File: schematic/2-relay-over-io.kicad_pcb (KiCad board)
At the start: 2 copper layers, 86.4 x 51.4 mm, 26 parts, among them J2 Screw_Terminal_01x03, J3 Screw_Terminal_01x03, J5 Conn_02x05_Odd_Even, J6 Conn_02x05_Odd_Even, J7 Conn_02x08_Odd_Even, J8 Conn_02x08_Odd_Even, Q2 BC817, Q3 BC817, U2 SONGLE_3V_relay, U3 SONGLE_3V_relay, U6 DizzyBITLogo, U7 DizzyBIT-Layout

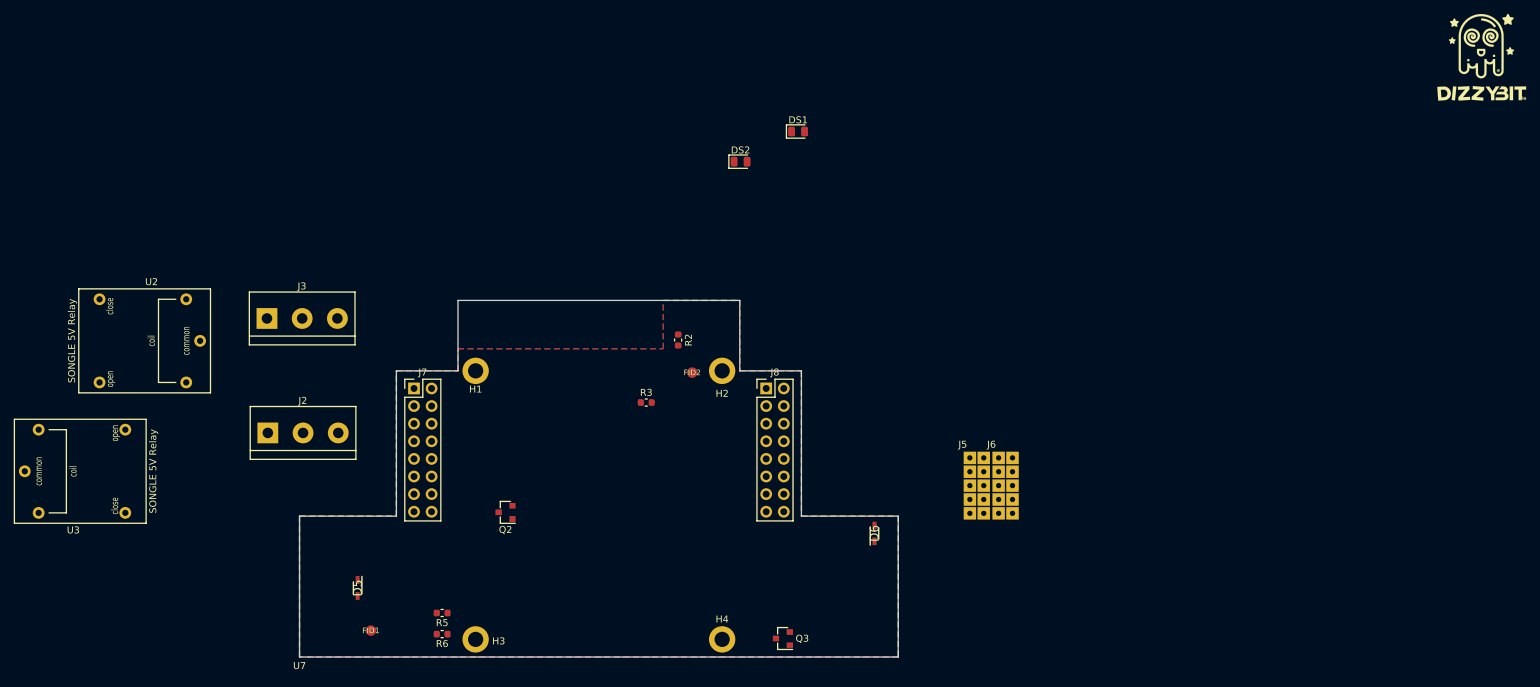
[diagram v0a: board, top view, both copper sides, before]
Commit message: Updated according to standard module design
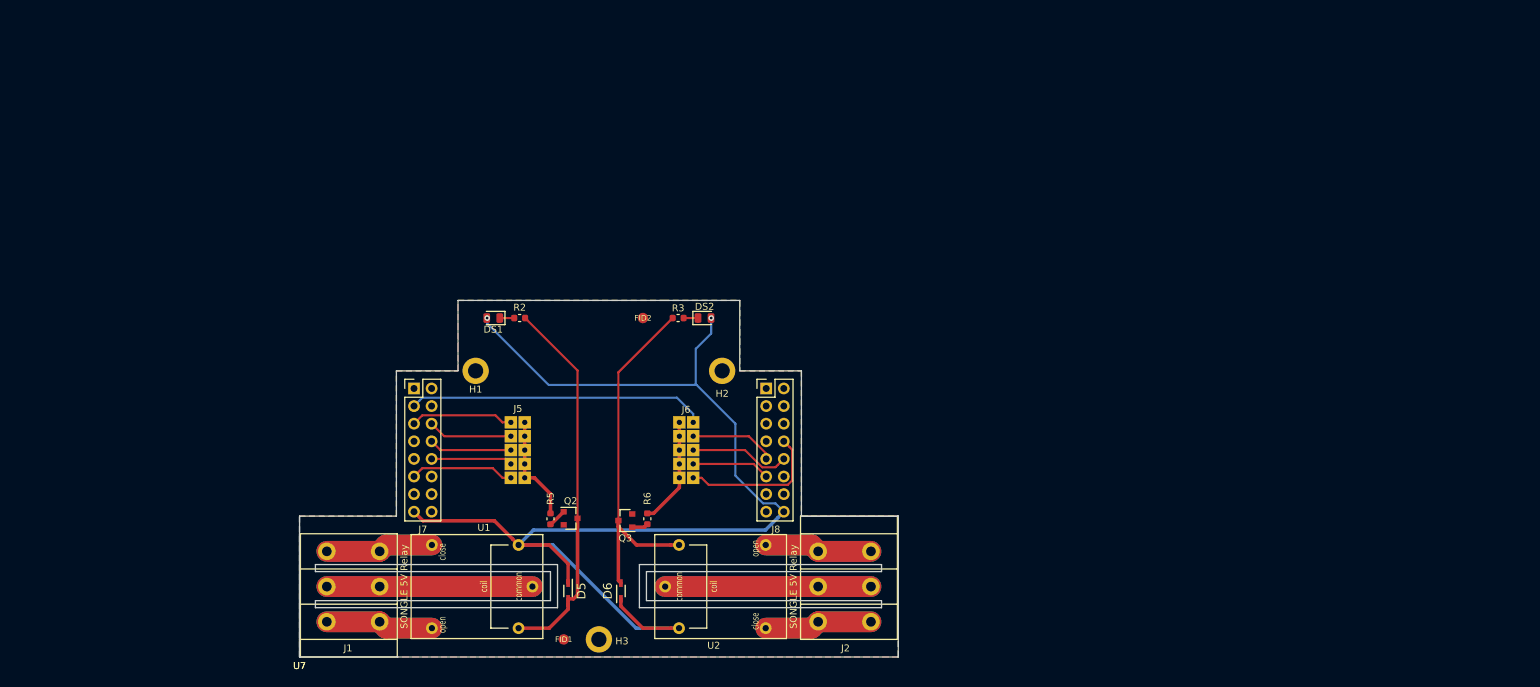
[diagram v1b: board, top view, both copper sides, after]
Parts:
- removed H4: MountingHole, MountingHole:MountingHole_2.2mm_M2_DIN965_Pad
- removed J3: Screw_Terminal_01x03, TerminalBlock:TerminalBlock_bornier-3_P5.08mm
- removed U3: SONGLE_3V_relay, Songle:SONGLE_5V_Relay
- removed the U7 at (76.2, 146.1)
- added J1: WJ142R-5.08-3P, TerminalBlock:WJ142R-5.08-3P, F.Cu at (90.3, 146.1)
- added U1: SONGLE_3V_relay, Songle:SONGLE_5V_Relay, F.Cu at (102.3, 135.4)
- added U7 (x2): DizzyBIT-Layout, DizzyBit:DizzyBit-Din Rail Module, F.Cu at (76.2, 146.1)
- J2: value Screw_Terminal_01x03 -> WJ142R-5.08-3P; footprint TerminalBlock:TerminalBlock_bornier-3_P5.08mm -> TerminalBlock:WJ142R-5.08-3P
- U6: moved to B.Cu
- moved U6 139.7 mm to (119.4, 117.0), turned to 180 degrees
- moved U2 89.8 mm to (136.4, 136.4), turned to 180 degrees
- moved J2 77.8 mm to (148.5, 125.7)
- moved J5 66.4 mm to (105.7, 111.2)
- moved DS1 51.6 mm to (104.1, 97.2), turned to 180 degrees
- moved J6 42.3 mm to (134.0, 121.2), turned to 180 degrees
- moved D6 37.5 mm to (122.6, 136.5)
- moved R6 33.9 mm to (126.4, 126.1), turned to 270 degrees
- moved D5 30.4 mm to (114.9, 136.5)
- moved Q3 28.4 mm to (123.2, 126.4)
- moved FID1 27.8 mm to (114.3, 143.5)
- moved DS2 23.1 mm to (134.6, 97.2)
- moved R2 23.1 mm to (108.0, 97.2), turned to 180 degrees
- moved R5 20.7 mm to (112.4, 126.1), turned to 270 degrees
- moved H3 17.8 mm to (119.4, 143.5)
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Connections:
- U2 pad 2: Net-(D5-Pad2) -> Net-(D6-Pad2)
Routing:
- net +3V3: track 0.00 -> 177.4 mm, vias 0 -> 2
- net Net-(J2-Pad2): track 0.00 -> 59.4 mm
- net Net-(J1-Pad2): track 0.00 -> 59.3 mm
- net Net-(D5-Pad2): track 0.00 -> 54.7 mm
- net Net-(D6-Pad2): track 0.00 -> 52.4 mm
- net IO33: track 0.00 -> 43.0 mm
- net Net-(J2-Pad1): track 0.00 -> 31.1 mm
- net Net-(J2-Pad3): track 0.00 -> 31.1 mm
- net Net-(J1-Pad3): track 0.00 -> 31.1 mm
- net Net-(J1-Pad1): track 0.00 -> 31.1 mm
- net IO5: track 0.00 -> 21.1 mm
- net RELAY2_CTR: track 0.00 -> 15.6 mm
- net RELAY1_CTR: track 0.00 -> 15.5 mm
- net IO15: track 0.00 -> 15.0 mm
- net IO26: track 0.00 -> 14.9 mm
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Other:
- outline, holes or cut-outs redrawn
- board text added: "2 Relay Module"
- board text added: "IO04"
- board text added: "IO05"
- board text added: "IO15"
- board text added: "IO16"
- board text added: "IO17"
- board text added: "IO25"
- board text added: "IO26"
- board text added: "IO27"
- board text added: "IO32"
- board text added: "IO33"
- board text added: "Relay 1 Control"
- board text added: "Relay 2 Control"
- board text removed: "ESP32D MCU"

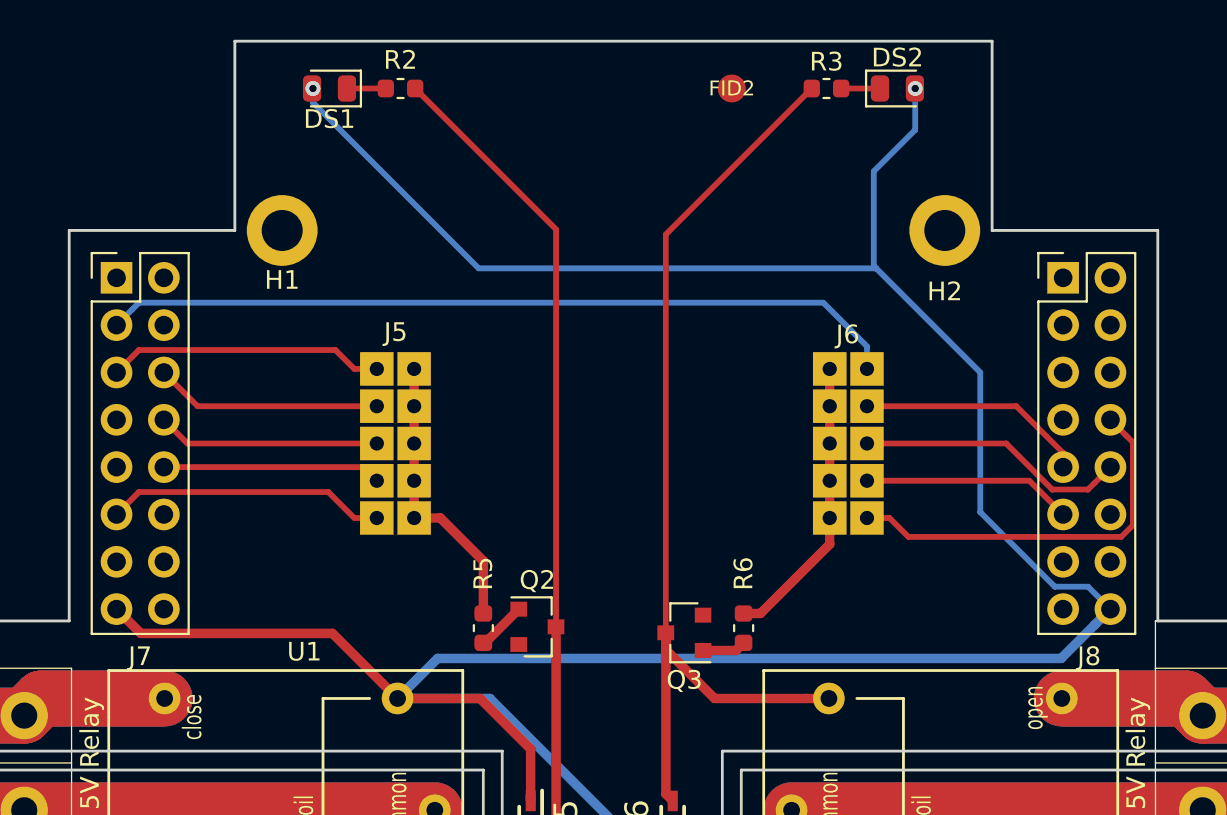
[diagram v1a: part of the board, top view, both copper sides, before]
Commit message: Updated 3.3v position and tracks
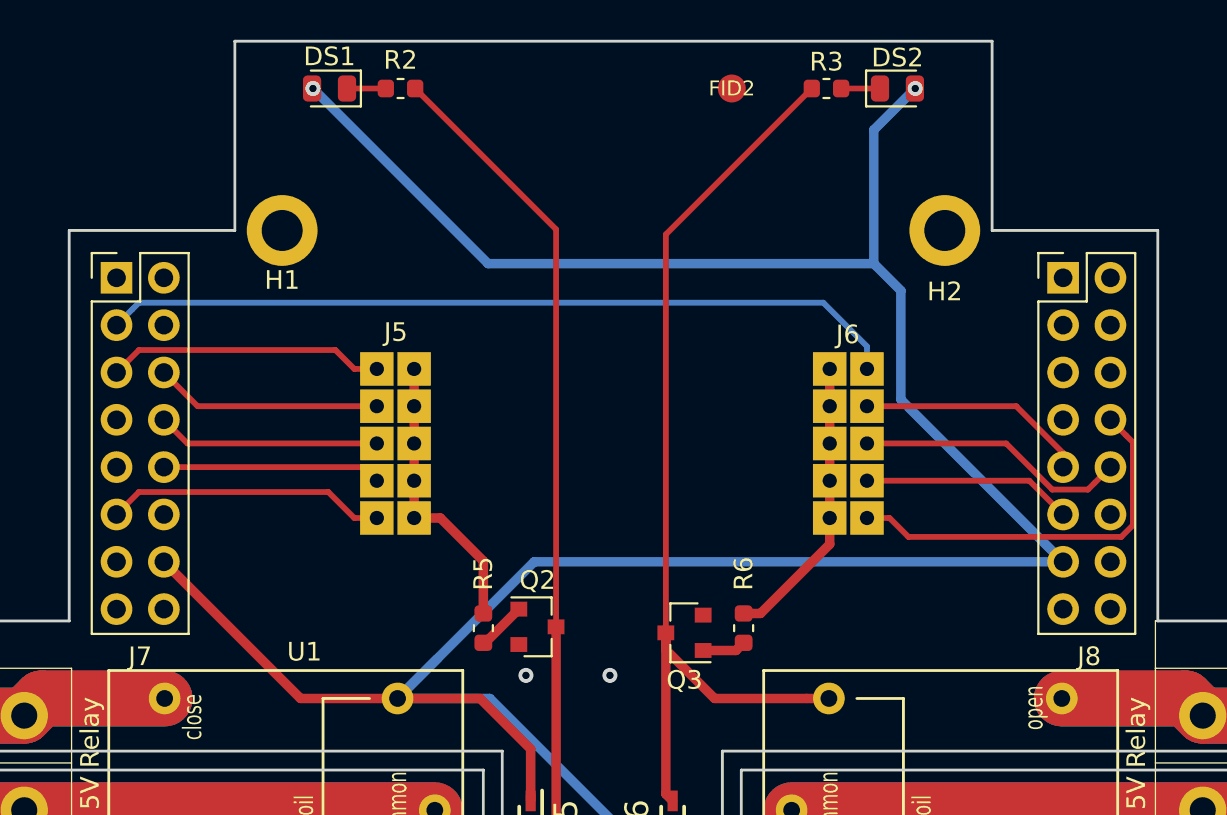
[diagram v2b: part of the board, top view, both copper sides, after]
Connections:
- J7 pad 14: (no net) -> +3V3
- J7 pad 15: +3V3 -> (no net)
- J8 pad 13: (no net) -> +3V3
- J8 pad 16: +3V3 -> (no net)
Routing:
- net +3V3: track 177.4 -> 172.4 mm
- net GND: vias 0 -> 2
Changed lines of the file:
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@@
-(kicad_pcb (version 20171130) (host pcbnew "(5.1.0)-1")
+(kicad_pcb (version 20171130) (host pcbnew "(5.0.2)-1")
   (general
     (thickness 1.6)
     (drawings 41)
-    (tracks 129)
+    (tracks 125)
     (zones 0)
     (modules 26)
@@
     (47 F.CrtYd user)
     (48 B.Fab user hide)
-    (49 F.Fab user)
+    (49 F.Fab user hide)
   )
   (setup
-    (last_trace_width 0.25)
+    (last_trace_width 0.508)
     (user_trace_width 0.254)
     (user_trace_width 0.31)
@@
     (zone_45_only no)
     (trace_min 0.2)
+    (segment_width 0.2)
+    (edge_width 0.15)
     (via_size 0.8)
     (via_drill 0.4)
@@
     (uvia_min_size 0.2)
     (uvia_min_drill 0.1)
-    (edge_width 0.15)
-    (segment_width 0.2)
     (pcb_text_width 0.3)
     (pcb_text_size 1.5 1.5)
@@
     (tags diode)
     (attr smd)
-    (fp_text reference DS1 (at 0 -1.65 180) (layer F.SilkS)
+    (fp_text reference DS1 (at 0 1.7145 180) (layer F.SilkS)
       (effects (font (size 1 1) (thickness 0.15)))
     )
@@
     (pad 12 thru_hole oval (at 2.54 12.7) (size 1.7 1.7) (drill 1) (layers *.Cu *.Mask))
     (pad 13 thru_hole oval (at 0 15.24) (size 1.7 1.7) (drill 1) (layers *.Cu *.Mask))
-    (pad 14 thru_hole oval (at 2.54 15.24) (size 1.7 1.7) (drill 1) (layers *.Cu *.Mask))
-    (pad 15 thru_hole oval (at 0 17.78) (size 1.7 1.7) (drill 1) (layers *.Cu *.Mask)
+    (pad 14 thru_hole oval (at 2.54 15.24) (size 1.7 1.7) (drill 1) (layers *.Cu *.Mask)
       (net 23 +3V3))
+    (pad 15 thru_hole oval (at 0 17.78) (size 1.7 1.7) (drill 1) (layers *.Cu *.Mask))
     (pad 16 thru_hole oval (at 2.54 17.78) (size 1.7 1.7) (drill 1) (layers *.Cu *.Mask)
       (net 1 GND))
@@
     (fp_line (start 3.81 -1.27) (end 3.81 19.05) (layer F.Fab) (width 0.1))
     (fp_line (start 0 -1.27) (end 3.81 -1.27) (layer F.Fab) (width 0.1))
-    (pad 16 thru_hole oval (at 2.54 17.78) (size 1.7 1.7) (drill 1) (layers *.Cu *.Mask)
-      (net 23 +3V3))
+    (pad 16 thru_hole oval (at 2.54 17.78) (size 1.7 1.7) (drill 1) (layers *.Cu *.Mask))
     (pad 15 thru_hole oval (at 0 17.78) (size 1.7 1.7) (drill 1) (layers *.Cu *.Mask)
       (net 1 GND))
     (pad 14 thru_hole oval (at 2.54 15.24) (size 1.7 1.7) (drill 1) (layers *.Cu *.Mask))
-    (pad 13 thru_hole oval (at 0 15.24) (size 1.7 1.7) (drill 1) (layers *.Cu *.Mask))
+    (pad 13 thru_hole oval (at 0 15.24) (size 1.7 1.7) (drill 1) (layers *.Cu *.Mask)
+      (net 23 +3V3))
     (pad 12 thru_hole oval (at 2.54 12.7) (size 1.7 1.7) (drill 1) (layers *.Cu *.Mask))
     (pad 11 thru_hole oval (at 0 12.7) (size 1.7 1.7) (drill 1) (layers *.Cu *.Mask)
@@
   (gr_line (start 162.56 146.05) (end 162.56 125.73) (layer Edge.Cuts) (width 0.15))
   (gr_line (start 76.2 146.05) (end 162.56 146.05) (layer Edge.Cuts) (width 0.15))
+  (via (at 119.1895 128.651) (size 0.8) (drill 0.4) (layers F.Cu B.Cu) (net 1))
+  (via (at 114.681 128.651) (size 0.8) (drill 0.4) (layers F.Cu B.Cu) (net 1))
   (segment (start 97.06 114.205) (end 106.68 114.205) (width 0.31) (layer F.Cu) (net 2))
   (segment (start 95.25 112.395) (end 97.06 114.205) (width 0.31) (layer F.Cu) (net 2))
@@
   (segment (start 130.985 120.205) (end 130.985 112.205) (width 0.508) (layer F.Cu) (net 22))
   (via (at 103.251 97.155) (size 0.8) (drill 0.4) (layers F.Cu B.Cu) (net 23))
+  (segment (start 133.35 106.553) (end 112.649 106.553) (width 0.508) (layer B.Cu) (net 23))
+  (segment (start 112.649 106.553) (end 103.251 97.155) (width 0.508) (layer B.Cu) (net 23))
   (via (at 135.5725 97.155) (size 0.8) (drill 0.4) (layers F.Cu B.Cu) (net 23))
-  (segment (start 106.941501 129.040001) (end 107.7915 129.89) (width 0.508) (layer F.Cu) (net 23))
-  (segment (start 104.300501 126.399001) (end 106.941501 129.040001) (width 0.508) (layer F.Cu) (net 23))
-  (segment (start 94.014001 126.399001) (end 104.300501 126.399001) (width 0.508) (layer F.Cu) (net 23))
-  (segment (start 92.71 125.095) (end 94.014001 126.399001) (width 0.508) (layer F.Cu) (net 23))
   (segment (start 107.7915 129.89) (end 112.745 129.89) (width 0.508) (layer B.Cu) (net 23))
   (segment (start 112.745 129.89) (end 124.745 141.89) (width 0.508) (layer B.Cu) (net 23))
   (segment (start 124.745 141.89) (end 130.94 141.89) (width 0.508) (layer B.Cu) (net 23))
   (segment (start 114.935 135.105) (end 114.935 135.385) (width 0.508) (layer F.Cu) (net 23))
-  (segment (start 144.844999 123.889999) (end 146.05 125.095) (width 0.31) (layer B.Cu) (net 23))
-  (segment (start 143.061597 123.889999) (end 144.844999 123.889999) (width 0.31) (layer B.Cu) (net 23))
-  (segment (start 135.5725 99.3775) (end 133.35 101.6) (width 0.31) (layer B.Cu) (net 23))
-  (segment (start 135.5725 97.155) (end 135.5725 99.3775) (width 0.31) (layer B.Cu) (net 23))
-  (segment (start 139.065 112.395) (end 139.065 119.893402) (width 0.31) (layer B.Cu) (net 23))
-  (segment (start 133.35 101.6) (end 133.35 106.68) (width 0.31) (layer B.Cu) (net 23))
-  (segment (start 139.065 119.893402) (end 143.061597 123.889999) (width 0.31) (layer B.Cu) (net 23))
   (segment (start 129.737919 141.89) (end 130.94 141.89) (width 0.508) (layer F.Cu) (net 23))
   (segment (start 125.717 141.89) (end 129.737919 141.89) (width 0.508) (layer F.Cu) (net 23))
@@
   (segment (start 112.223133 129.89) (end 107.7915 129.89) (width 0.508) (layer F.Cu) (net 23))
   (segment (start 114.935 132.601867) (end 112.223133 129.89) (width 0.508) (layer F.Cu) (net 23))
-  (segment (start 103.251 97.155) (end 103.251 97.917) (width 0.31) (layer B.Cu) (net 23))
-  (segment (start 112.141 106.807) (end 133.477 106.807) (width 0.31) (layer B.Cu) (net 23))
-  (segment (start 103.251 97.917) (end 112.141 106.807) (width 0.31) (layer B.Cu) (net 23))
   (segment (start 133.35 106.68) (end 133.477 106.807) (width 0.31) (layer B.Cu) (net 23))
-  (segment (start 133.477 106.807) (end 139.065 112.395) (width 0.31) (layer B.Cu) (net 23))
-  (segment (start 145.200001 125.944999) (end 146.05 125.095) (width 0.508) (layer B.Cu) (net 23))
-  (segment (start 143.40401 127.74099) (end 145.200001 125.944999) (width 0.508) (layer B.Cu) (net 23))
-  (segment (start 109.94051 127.74099) (end 143.40401 127.74099) (width 0.508) (layer B.Cu) (net 23))
   (segment (start 107.7915 129.89) (end 109.94051 127.74099) (width 0.508) (layer B.Cu) (net 23))
+  (segment (start 102.585 129.89) (end 107.7915 129.89) (width 0.508) (layer F.Cu) (net 23))
+  (segment (start 95.25 122.555) (end 102.585 129.89) (width 0.508) (layer F.Cu) (net 23))
+  (segment (start 115.1265 122.555) (end 143.51 122.555) (width 0.508) (layer B.Cu) (net 23))
+  (segment (start 107.7915 129.89) (end 115.1265 122.555) (width 0.508) (layer B.Cu) (net 23))
+  (segment (start 134.805999 108.008999) (end 133.35 106.553) (width 0.508) (layer B.Cu) (net 23))
+  (segment (start 134.805999 113.850999) (end 134.805999 108.008999) (width 0.508) (layer B.Cu) (net 23))
+  (segment (start 143.51 122.555) (end 134.805999 113.850999) (width 0.508) (layer B.Cu) (net 23))
+  (segment (start 133.35 106.553) (end 133.35 106.68) (width 0.31) (layer B.Cu) (net 23))
+  (segment (start 133.35 99.3775) (end 135.5725 97.155) (width 0.508) (layer B.Cu) (net 23))
+  (segment (start 133.35 106.553) (end 133.35 99.3775) (width 0.508) (layer B.Cu) (net 23))
   (segment (start 80.137 140.97) (end 87.757 140.97) (width 3) (layer F.Cu) (net 24))
   (segment (start 88.677 141.89) (end 87.757 140.97) (width 3) (layer F.Cu) (net 24))
